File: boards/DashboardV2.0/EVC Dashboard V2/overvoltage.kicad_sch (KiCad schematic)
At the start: 0 parts

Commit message: Dashboard schematic changes
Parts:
- added U2: ADP3338AKCZ, KC_3_ADI, symbol Regulators:ADP3338AKCZ
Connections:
- new net GND: U2.1 (GND)
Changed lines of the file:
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@@
 	(generator_version "10.0")
 	(paper "A4")
+	(symbol
+		(lib_id "Regulators:ADP3338AKCZ")
+		(at 33.02 44.45 0)
+		(unit 1)
+		(body_style 1)
+		(exclude_from_sim no)
+		(in_bom yes)
+		(on_board yes)
+		(in_pos_files yes)
+		(dnp no)
+		(fields_autoplaced yes)
+		(property "Reference" "U2"
+			(at 66.04 24.13 0)
+			(show_name no)
+			(do_not_autoplace no)
+			(effects
+				(font
+					(size 1.524 1.524)
+				)
+			)
+		)
+		(property "Value" "ADP3338AKCZ"
+			(at 66.04 26.67 0)
+			(show_name no)
+			(do_not_autoplace no)
+			(effects
+				(font
+					(size 1.524 1.524)
+				)
+			)
+		)
+		(property "Footprint" "KC_3_ADI"
+			(at 33.02 44.45 0)
+			(hide yes)
+			(show_name no)
+			(do_not_autoplace no)
+			(effects
+				(font
+					(size 1.27 1.27)
+					(italic yes)
+				)
+			)
+		)
+		(property "Datasheet" "https://www.analog.com/media/en/technical-documentation/data-sheets/ADP3338.pdf"
+			(at 33.02 44.45 0)
+			(hide yes)
+			(show_name no)
+			(do_not_autoplace no)
+			(effects
+				(font
+					(size 1.27 1.27)
+					(italic yes)
+				)
+			)
+		)
+		(property "Description" ""
+			(at 33.02 44.45 0)
+			(hide yes)
+			(show_name no)
+			(do_not_autoplace no)
+			(effects
+				(font
+					(size 1.27 1.27)
+				)
+			)
+		)
+		(pin "1"
+		)
+		(pin "2"
+		)
+		(pin "3"
+		)
+		(instances
+			(project "EVC Dashboard V2"
+				(path "/ede78d5d-1d5c-4e8d-a13e-c039265851a9/a863baeb-ace9-4290-ba79-a0c3a9791cc4"
+					(reference "U2")
+					(unit 1)
+				)
+			)
+		)
+	)
+	(symbol
+		(lib_id "power:GND")
+		(at 33.02 44.45 0)
+		(unit 1)
+		(body_style 1)
+		(exclude_from_sim no)
+		(in_bom yes)
+		(on_board yes)
+		(in_pos_files yes)
+		(dnp no)
+		(fields_autoplaced yes)
+		(property "Reference" "#PWR05"
+			(at 33.02 50.8 0)
+			(hide yes)
+			(show_name no)
+			(do_not_autoplace no)
+			(effects
+				(font
+					(size 1.27 1.27)
+				)
+			)
+		)
+		(property "Value" "GND"
+			(at 33.02 49.53 0)
+			(show_name no)
+			(do_not_autoplace no)
+			(effects
+				(font
+					(size 1.27 1.27)
+				)
+			)
+		)
+		(property "Footprint" ""
+			(at 33.02 44.45 0)
+			(hide yes)
+			(show_name no)
+			(do_not_autoplace no)
+			(effects
+				(font
+					(size 1.27 1.27)
+				)
+			)
+		)
+		(property "Datasheet" ""
+			(at 33.02 44.45 0)
+			(hide yes)
+			(show_name no)
+			(do_not_autoplace no)
+			(effects
+				(font
+					(size 1.27 1.27)
+				)
+			)
+		)
+		(property "Description" "Power symbol creates a global label with name \"GND\" , ground"
+			(at 33.02 44.45 0)
+			(hide yes)
+			(show_name no)
+			(do_not_autoplace no)
+			(effects
+				(font
+					(size 1.27 1.27)
+				)
+			)
+		)
+		(pin "1"
+		)
+		(instances
+			(project "EVC Dashboard V2"
+				(path "/ede78d5d-1d5c-4e8d-a13e-c039265851a9/a863baeb-ace9-4290-ba79-a0c3a9791cc4"
+					(reference "#PWR05")
+					(unit 1)
+				)
+			)
+		)
+	)
 )

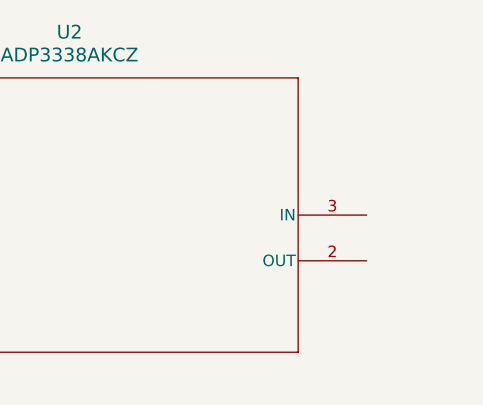
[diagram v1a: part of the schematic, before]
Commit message: Dashboard schematic changes
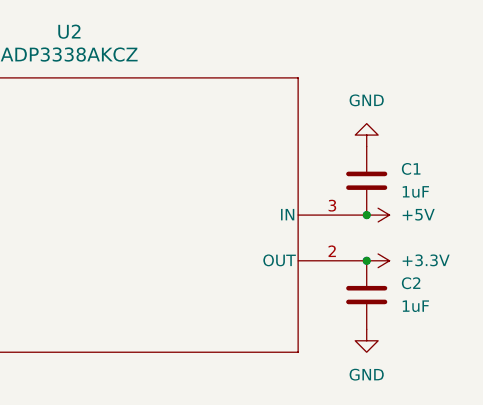
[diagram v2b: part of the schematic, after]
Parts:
- added C1, C2: 1uF, symbol Device:C
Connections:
- net GND: now also C1.1, C2.2
- net +3.3V: now reaches U2.2 (OUT)
- net +3.3V: now also C2.1
- net +5V: now reaches U2.3 (IN)
- net +5V: now also C1.2

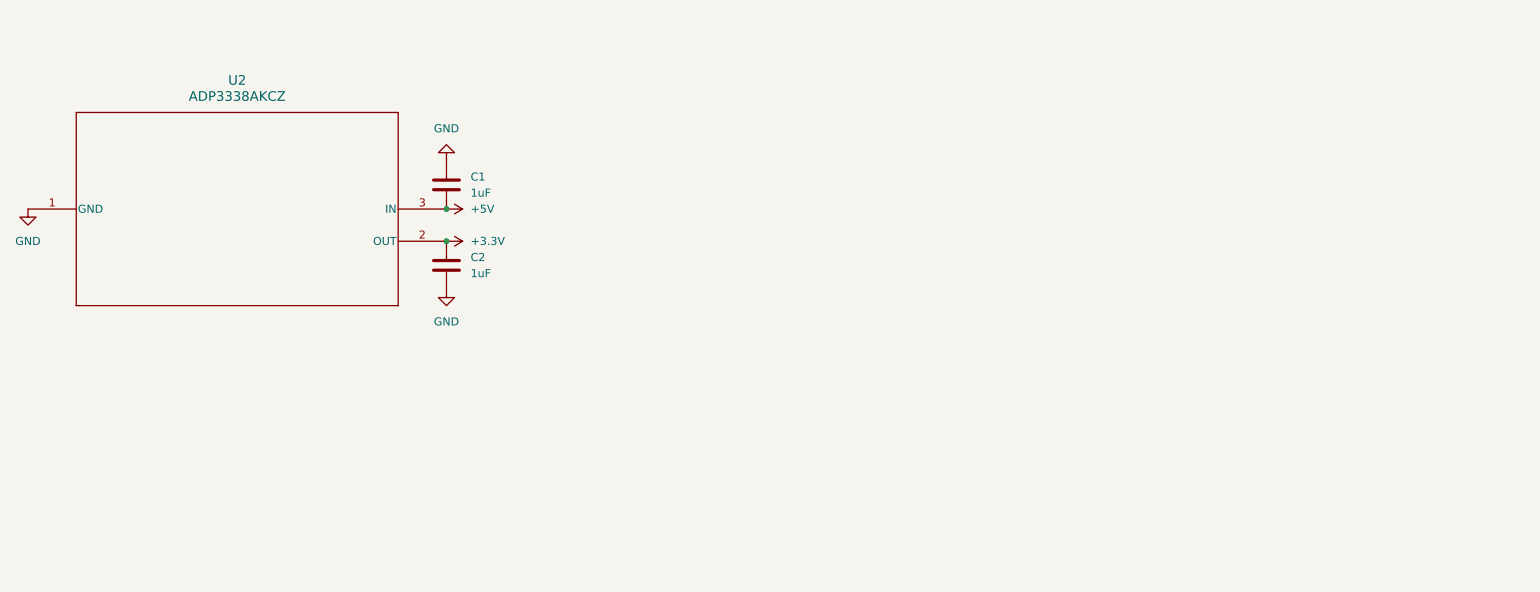
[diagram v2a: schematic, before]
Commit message: Overvoltage Protection component & mosfet addition
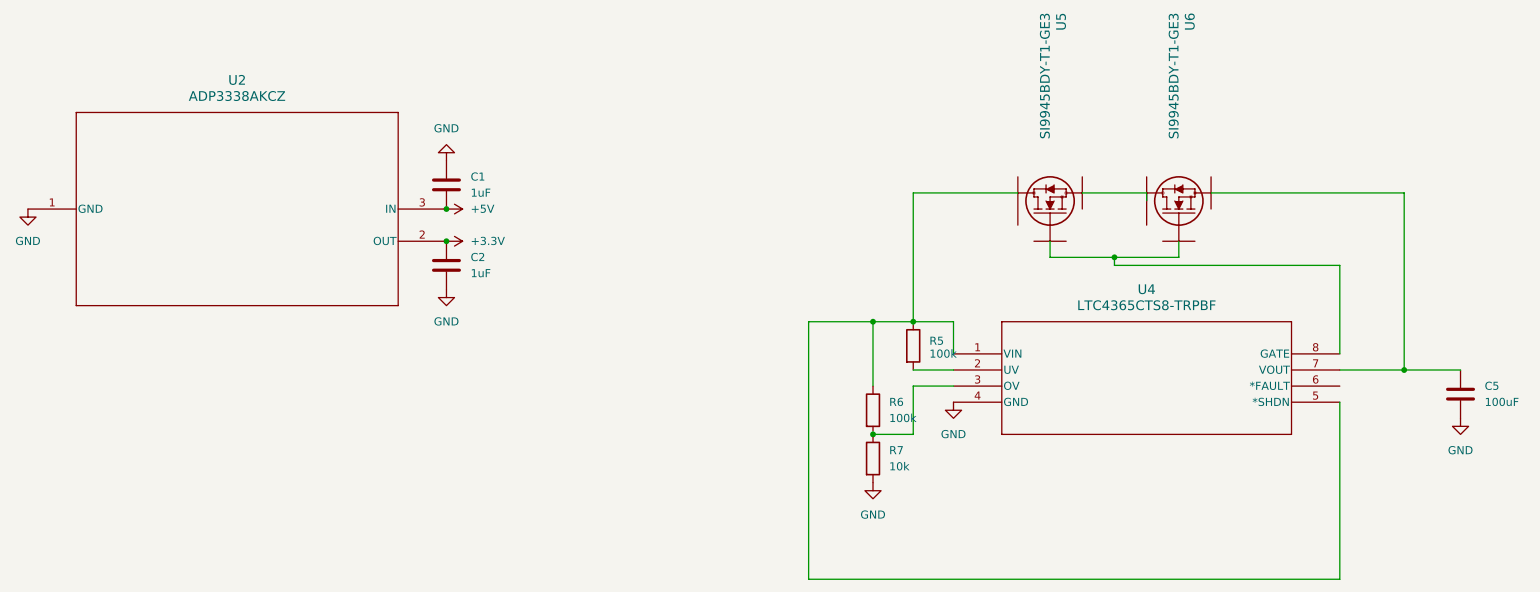
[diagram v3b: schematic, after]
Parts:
- added C5: 100uF, symbol Device:C
- added R5, R6: 100k, symbol Device:R
- added R7: 10k, symbol Device:R
- added U4: LTC4365CTS8-TRPBF, TSOT-23_TS8_LIT, symbol Regulators:LTC4365CTS8-TRPBF
- added U5, U6: SI9945BDY-T1-GE3, SOIC_T1-GE3_VIS, symbol SI9945BDY-T1-GE3:SI9945BDY-T1-GE3
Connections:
- net GND: now also C5.2, R7.2, U4.4 (GND)
- new net: R6.2, R7.1, U4.3 (OV)
- new net: R5.1, R6.1, U4.1 (VIN), U4.5 (*SHDN)
- new net: R5.2, U4.2 (UV)
- new net: C5.1, U4.7 (VOUT)

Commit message: 5V label
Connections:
- net +5V is gone; now on net P_5v: C1.2, U2.3 (IN)
- net P_5v: now reaches C5.1, U4.7 (VOUT)
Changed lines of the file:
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@@
-	)
-	(junction
-		(at 99.06 44.45)
-		(diameter 0)
-		(color 0 0 0 0)
 	)
 	(junction
@@
 			(width 0)
 			(type default)
+		)
+	)
+	(global_label "P_5v"
+		(shape input)
+		(at 99.06 44.45 0)
+		(fields_autoplaced yes)
+		(effects
+			(font
+				(size 1.27 1.27)
+			)
+			(justify left)
+		)
+		(property "Intersheetrefs" "${INTERSHEET_REFS}"
+			(at 106.4599 44.45 0)
+			(hide yes)
+			(show_name no)
+			(do_not_autoplace no)
+			(effects
+				(font
+					(size 1.27 1.27)
+				)
+				(justify left)
+			)
+		)
+	)
+	(global_label "P_5v"
+		(shape input)
+		(at 259.08 69.85 0)
+		(fields_autoplaced yes)
+		(effects
+			(font
+				(size 1.27 1.27)
+			)
+			(justify left)
+		)
+		(property "Intersheetrefs" "${INTERSHEET_REFS}"
+			(at 266.4799 69.85 0)
+			(hide yes)
+			(show_name no)
+			(do_not_autoplace no)
+			(effects
+				(font
+					(size 1.27 1.27)
+				)
+				(justify left)
+			)
 		)
 	)
@@
 					(unit 1)
 				)
-			)
-		)
-	)
-	(symbol
-		(lib_id "power:+5V")
-		(at 99.06 44.45 270)
-		(unit 1)
-		(body_style 1)
-		(exclude_from_sim no)
-		(in_bom yes)
-		(on_board yes)
-		(in_pos_files yes)
-		(dnp no)
-		(fields_autoplaced yes)
-		(property "Reference" "#PWR06"
-			(at 95.25 44.45 0)
-			(hide yes)
-			(show_name no)
-			(do_not_autoplace no)
-			(effects
-				(font
-					(size 1.27 1.27)
-				)
-			)
-		)
-		(property "Value" "+5V"
-			(at 102.87 44.4499 90)
-			(show_name no)
-			(do_not_autoplace no)
-			(effects
-				(font
-					(size 1.27 1.27)
-				)
-				(justify left)
-			)
-		)
-		(property "Footprint" ""
-			(at 99.06 44.45 0)
-			(hide yes)
-			(show_name no)
-			(do_not_autoplace no)
-			(effects
-				(font
-					(size 1.27 1.27)
-				)
-			)
-		)
-		(property "Datasheet" ""
-			(at 99.06 44.45 0)
-			(hide yes)
-			(show_name no)
-			(do_not_autoplace no)
-			(effects
-				(font
-					(size 1.27 1.27)
-				)
-			)
-		)
-		(property "Description" "Power symbol creates a global label with name \"+5V\""
-			(at 99.06 44.45 0)
-			(hide yes)
-			(show_name no)
-			(do_not_autoplace no)
-			(effects
-				(font
-					(size 1.27 1.27)
-				)
-			)
-		)
-		(pin "1"
-		)
-		(instances
-			(project "EVC Dashboard V2"
-				(path "/ede78d5d-1d5c-4e8d-a13e-c039265851a9/a863baeb-ace9-4290-ba79-a0c3a9791cc4"
-					(reference "#PWR06")
-					(unit 1)
-				)
